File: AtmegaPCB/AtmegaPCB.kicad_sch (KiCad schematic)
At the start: 19 parts

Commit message: Matrix done!
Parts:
- added D? (x74): SOD-123, symbol Device:D_Small
- added D?: (no value), symbol Device:D_Small
- added MX? (x74): MX-NoLED, symbol MX_Alps_Hybrid:MX-NoLED
- added MX?: (no value), symbol MX_Alps_Hybrid:MX-NoLED
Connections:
- new net: D?.2 (A), MX?.2 (ROW) (x75)
- new net COL0: MX?.1 (COL), MX?.1 (COL), MX?.1 (COL), MX?.1 (COL), MX?.1 (COL)
- new net COL1: MX?.1 (COL), MX?.1 (COL), MX?.1 (COL), MX?.1 (COL), MX?.1 (COL)
- new net COL10: MX?.1 (COL), MX?.1 (COL), MX?.1 (COL), MX?.1 (COL), MX?.1 (COL)
- new net COL11: MX?.1 (COL), MX?.1 (COL), MX?.1 (COL), MX?.1 (COL)
- new net COL12: MX?.1 (COL), MX?.1 (COL), MX?.1 (COL), MX?.1 (COL)
- new net COL13: MX?.1 (COL), MX?.1 (COL), MX?.1 (COL), MX?.1 (COL)
- new net COL14: MX?.1 (COL), MX?.1 (COL), MX?.1 (COL)
- new net COL15: MX?.1 (COL), MX?.1 (COL)
- new net COL16: MX?.1 (COL), MX?.1 (COL)
- new net COL17: MX?.1 (COL)
- new net COL2: MX?.1 (COL), MX?.1 (COL), MX?.1 (COL), MX?.1 (COL), MX?.1 (COL)
- new net COL3: MX?.1 (COL), MX?.1 (COL), MX?.1 (COL), MX?.1 (COL), MX?.1 (COL)
- new net COL4: MX?.1 (COL), MX?.1 (COL), MX?.1 (COL), MX?.1 (COL), MX?.1 (COL)
- new net COL5: MX?.1 (COL), MX?.1 (COL), MX?.1 (COL), MX?.1 (COL), MX?.1 (COL)
- new net COL6: MX?.1 (COL), MX?.1 (COL), MX?.1 (COL), MX?.1 (COL), MX?.1 (COL)
- new net COL7: MX?.1 (COL), MX?.1 (COL), MX?.1 (COL), MX?.1 (COL), MX?.1 (COL)
- new net COL8: MX?.1 (COL), MX?.1 (COL), MX?.1 (COL), MX?.1 (COL), MX?.1 (COL)
- new net COL9: MX?.1 (COL), MX?.1 (COL), MX?.1 (COL), MX?.1 (COL), MX?.1 (COL)
- new net ROW0: D?.1 (K), D?.1 (K), D?.1 (K), D?.1 (K), D?.1 (K), D?.1 (K), D?.1 (K), D?.1 (K), D?.1 (K), D?.1 (K), D?.1 (K), D?.1 (K), D?.1 (K), D?.1 (K), D?.1 (K), D?.1 (K), D?.1 (K), D?.1 (K)
- new net ROW1: D?.1 (K), D?.1 (K), D?.1 (K), D?.1 (K), D?.1 (K), D?.1 (K), D?.1 (K), D?.1 (K), D?.1 (K), D?.1 (K), D?.1 (K), D?.1 (K), D?.1 (K), D?.1 (K), D?.1 (K), D?.1 (K), D?.1 (K)
- new net ROW2: D?.1 (K), D?.1 (K), D?.1 (K), D?.1 (K), D?.1 (K), D?.1 (K), D?.1 (K), D?.1 (K), D?.1 (K), D?.1 (K), D?.1 (K), D?.1 (K), D?.1 (K), D?.1 (K)
- new net ROW3: D?.1 (K), D?.1 (K), D?.1 (K), D?.1 (K), D?.1 (K), D?.1 (K), D?.1 (K), D?.1 (K), D?.1 (K), D?.1 (K), D?.1 (K), D?.1 (K), D?.1 (K), D?.1 (K), D?.1 (K)
- new net ROW4: D?.1 (K), D?.1 (K), D?.1 (K), D?.1 (K), D?.1 (K), D?.1 (K), D?.1 (K), D?.1 (K), D?.1 (K), D?.1 (K), D?.1 (K)
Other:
- moved on the sheet: C?, F?, R?, SW?, U?, USB?, Y?

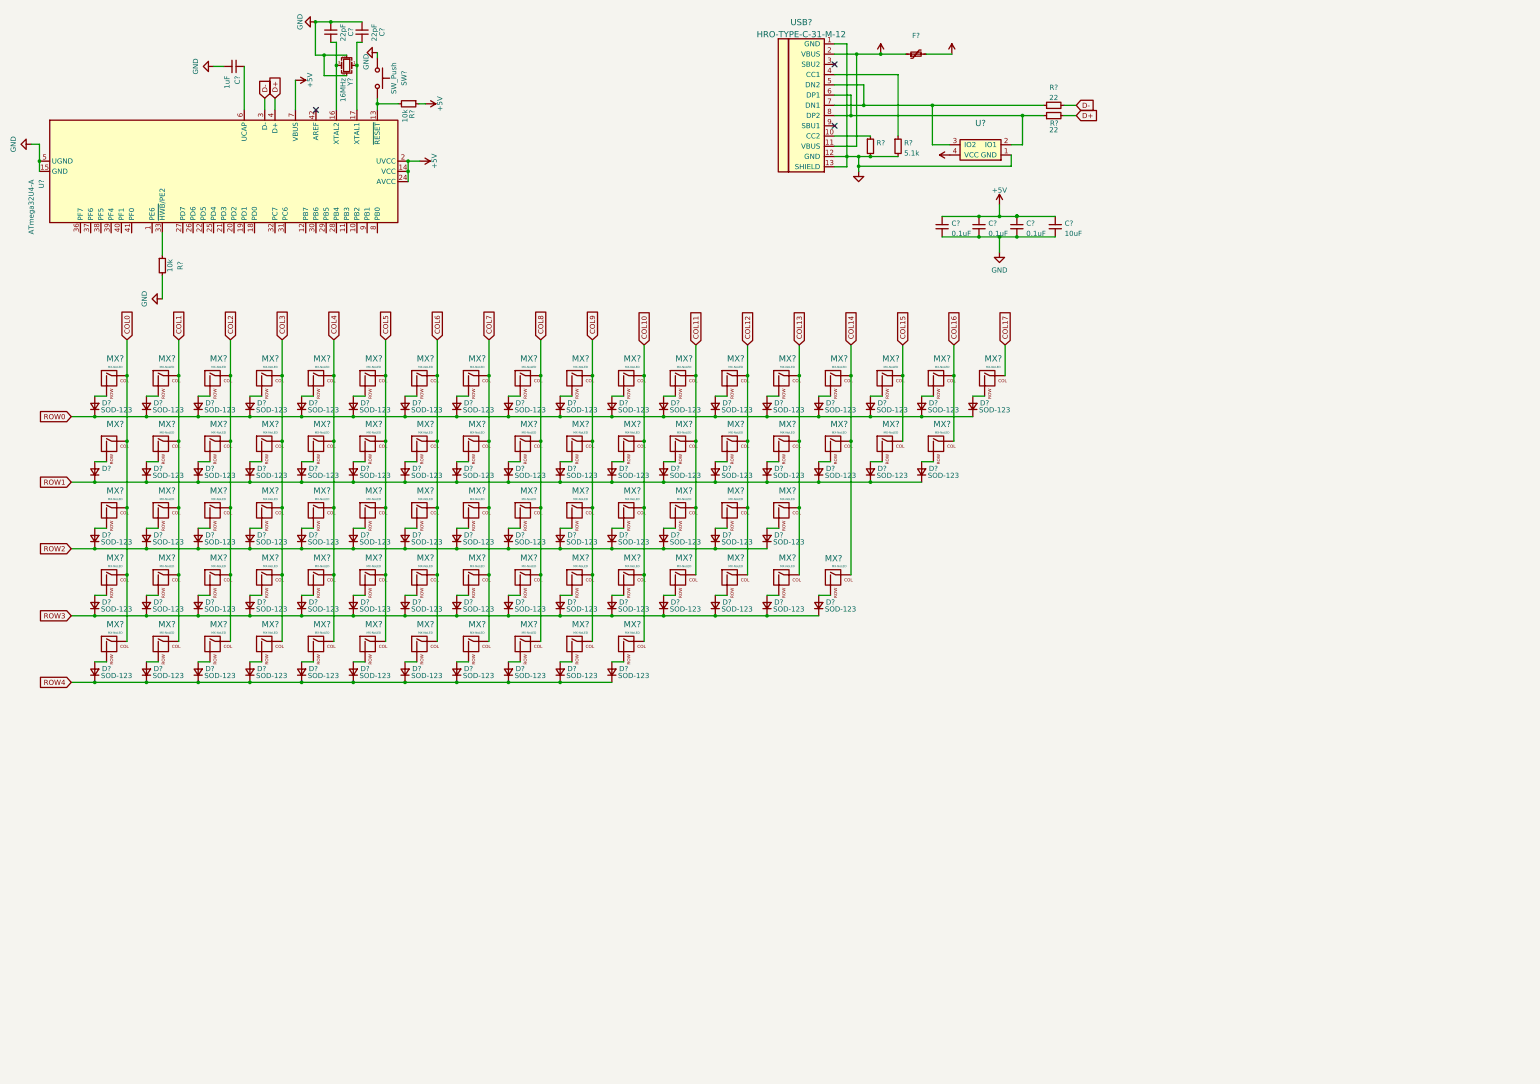
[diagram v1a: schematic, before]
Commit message: Added footprints
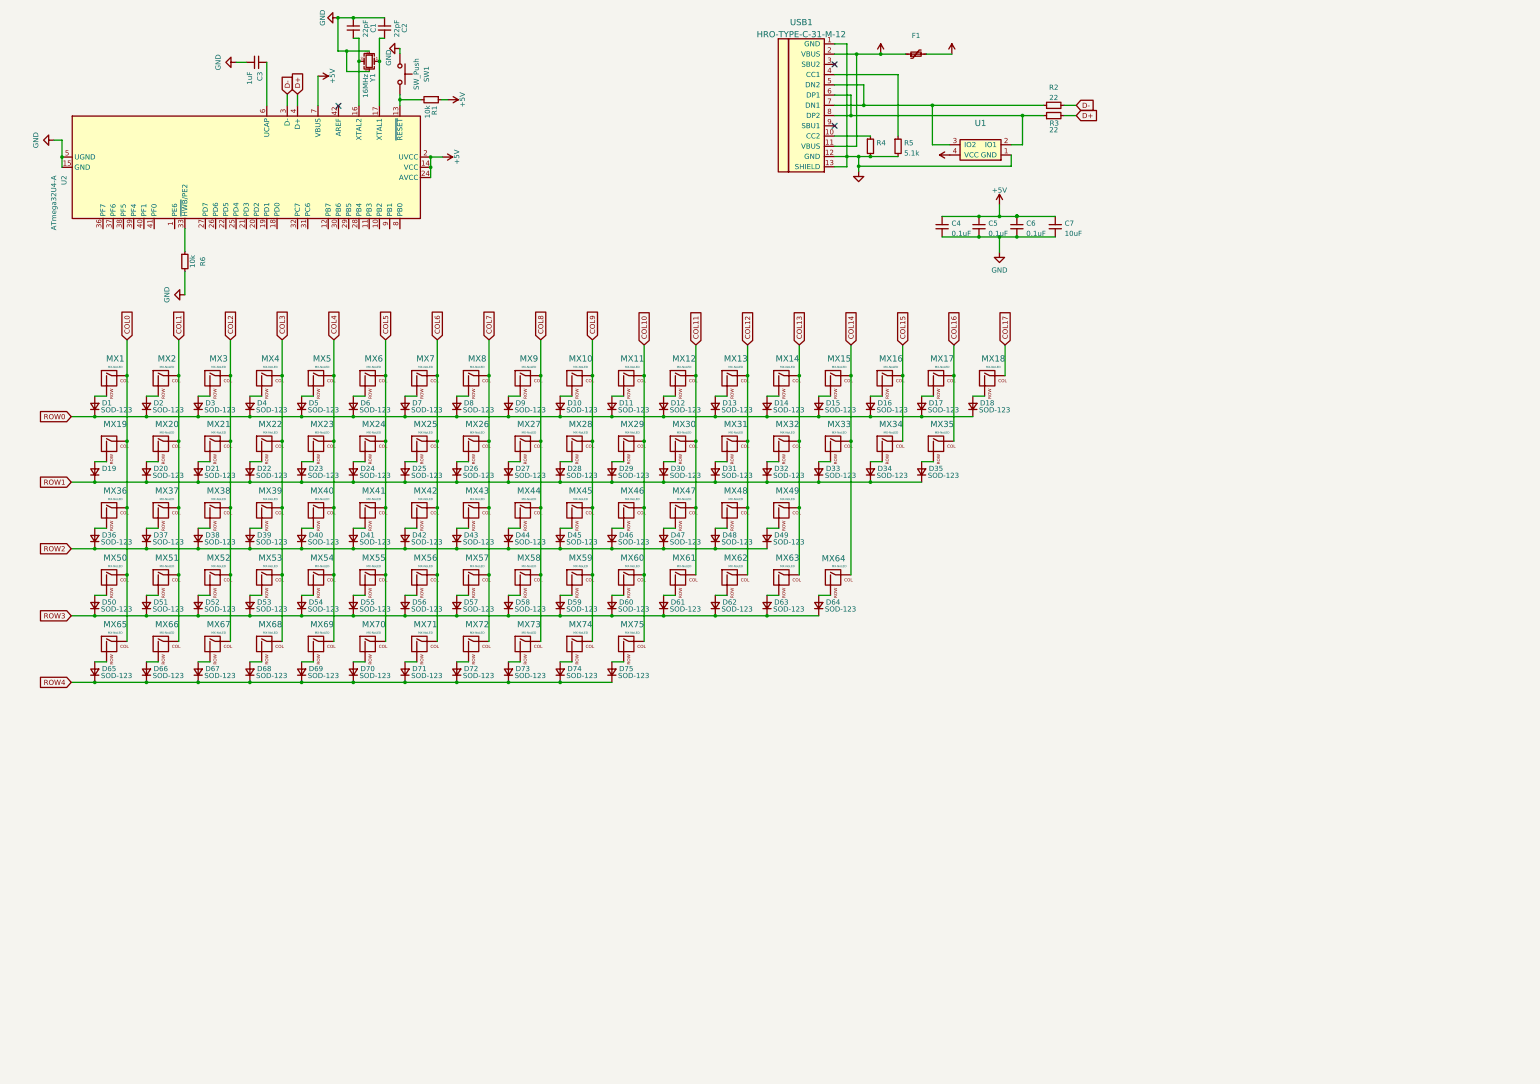
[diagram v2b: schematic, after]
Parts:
- gave numbers to parts that had none: 169
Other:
- moved on the sheet: C1, C2, C3, R1, R6, SW1, U2, Y1

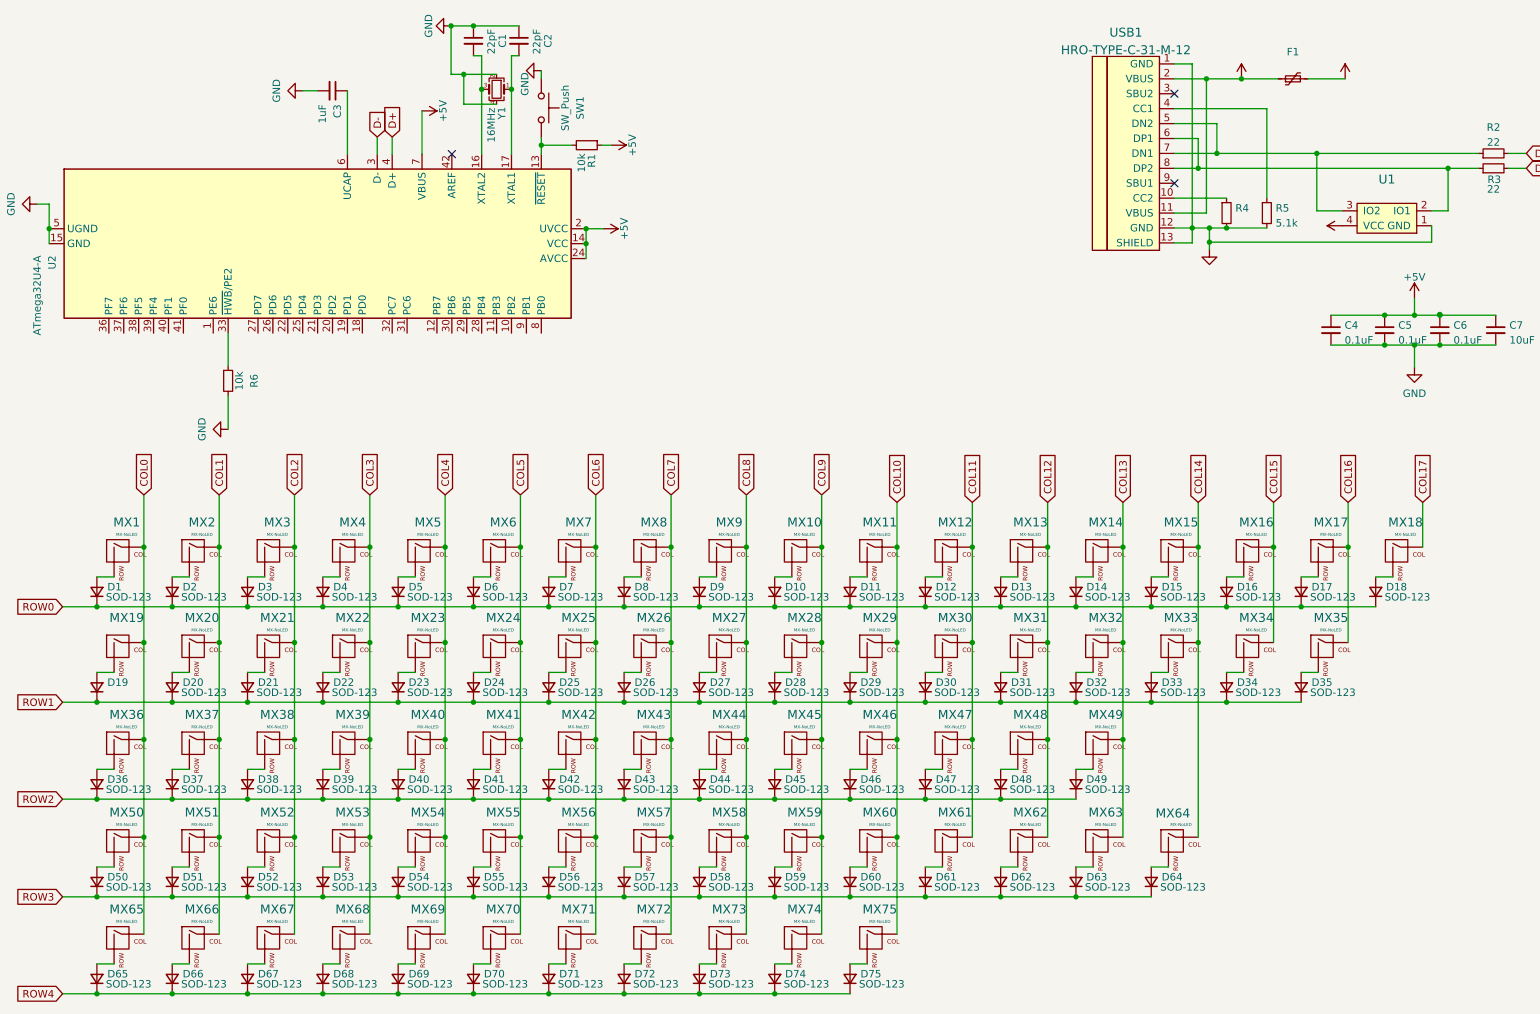
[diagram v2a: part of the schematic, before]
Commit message: Added missed keys
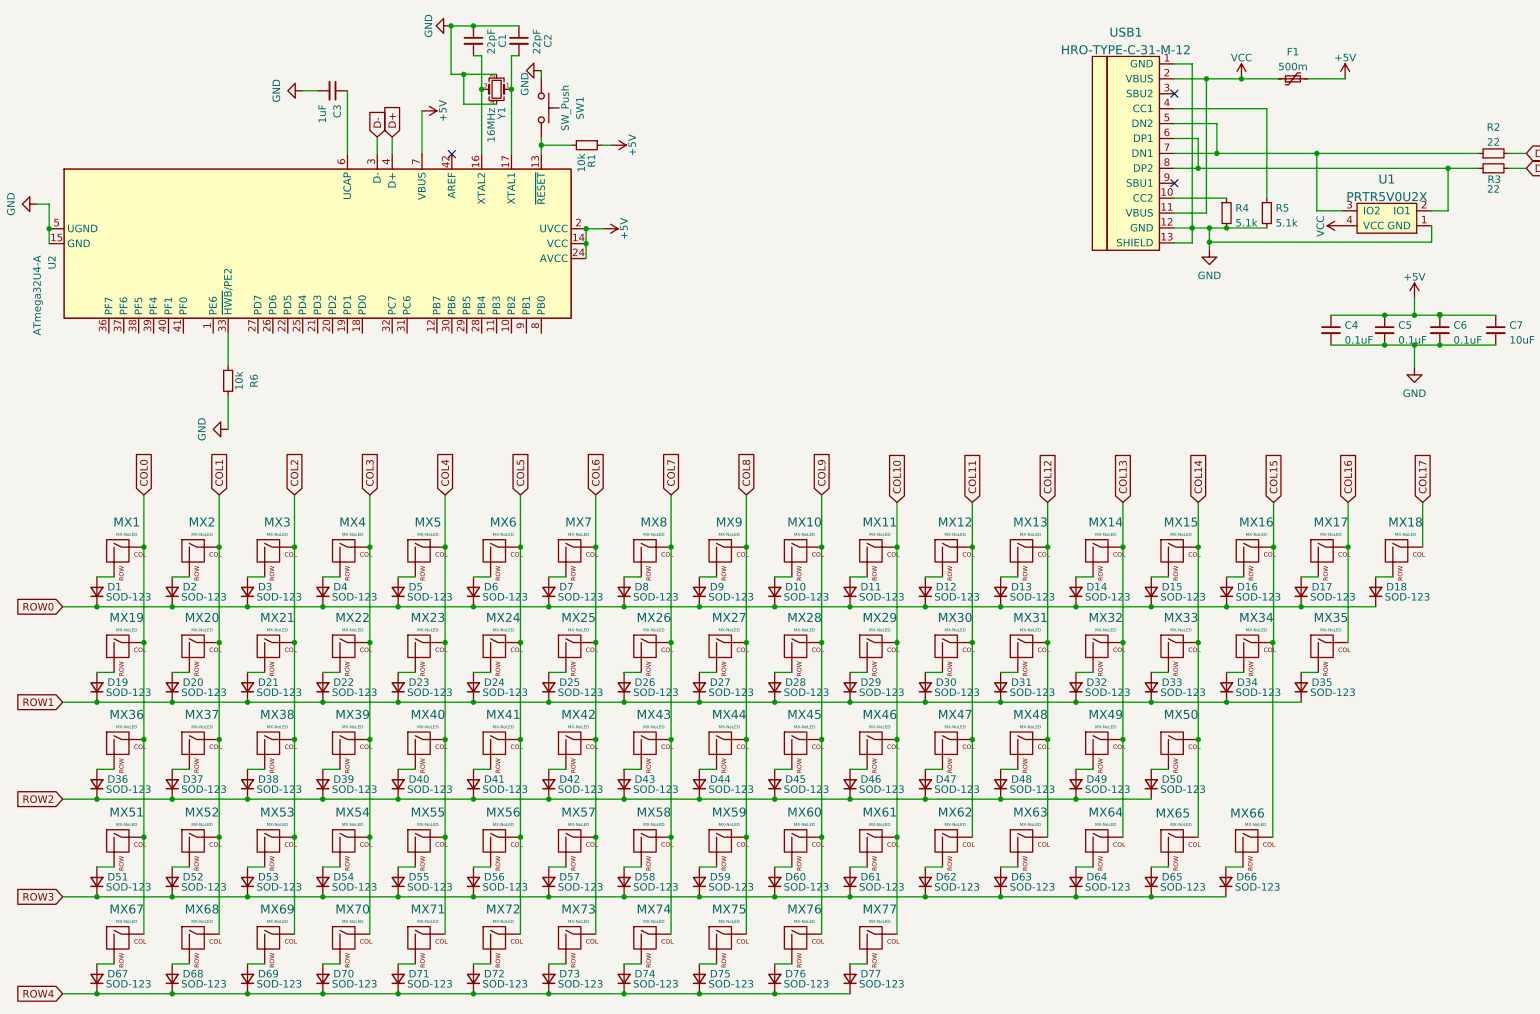
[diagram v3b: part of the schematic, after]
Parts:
- added D50, D66: SOD-123, Diode_SMD:D_SOD-123, symbol Device:D_Small
- added MX50: (no value), symbol MX_Alps_Hybrid:MX-NoLED
- added MX66: MX-NoLED, MX_Alps_Hybrid:MX-1U-NoLED, symbol MX_Alps_Hybrid:MX-NoLED
- C1, C2, C3, C4, C5, C6, C7: footprint (none) -> Capacitor_SMD:C_0805_2012Metric
- D1, D10, D11, D12, D13, D14, D15, D16, D17, D18, D2, D20, D21, D22, D23, D24, D25, D26, D27, D28, D29, D3, D30, D31, D32, D33, D34, D35, D36, D37, D38, D39, D4, D40, D41, D42, D43, D44, D45, D46, D47, D48, D49, D5, D6, D7, D8, D9: footprint (none) -> Diode_SMD:D_SOD-123
- D19: value (none) -> SOD-123; footprint (none) -> Diode_SMD:D_SOD-123
- D51: renamed from D50; footprint (none) -> Diode_SMD:D_SOD-123
- D52: renamed from D51; footprint (none) -> Diode_SMD:D_SOD-123
- D53: renamed from D52; footprint (none) -> Diode_SMD:D_SOD-123
- D54: renamed from D53; footprint (none) -> Diode_SMD:D_SOD-123
- D55: renamed from D54; footprint (none) -> Diode_SMD:D_SOD-123
- D56: renamed from D55; footprint (none) -> Diode_SMD:D_SOD-123
- D57: renamed from D56; footprint (none) -> Diode_SMD:D_SOD-123
- D58: renamed from D57; footprint (none) -> Diode_SMD:D_SOD-123
- D59: renamed from D58; footprint (none) -> Diode_SMD:D_SOD-123
- D60: renamed from D59; footprint (none) -> Diode_SMD:D_SOD-123
- D61: renamed from D60; footprint (none) -> Diode_SMD:D_SOD-123
- D62: renamed from D61; footprint (none) -> Diode_SMD:D_SOD-123
- D63: renamed from D62; footprint (none) -> Diode_SMD:D_SOD-123
- D64: renamed from D63; footprint (none) -> Diode_SMD:D_SOD-123
- D65: renamed from D64; footprint (none) -> Diode_SMD:D_SOD-123
- D67: renamed from D65; footprint (none) -> Diode_SMD:D_SOD-123
- D68: renamed from D66; footprint (none) -> Diode_SMD:D_SOD-123
- D69: renamed from D67; footprint (none) -> Diode_SMD:D_SOD-123
- D70: renamed from D68; footprint (none) -> Diode_SMD:D_SOD-123
- D71: renamed from D69; footprint (none) -> Diode_SMD:D_SOD-123
- D72: renamed from D70; footprint (none) -> Diode_SMD:D_SOD-123
- D73: renamed from D71; footprint (none) -> Diode_SMD:D_SOD-123
- D74: renamed from D72; footprint (none) -> Diode_SMD:D_SOD-123
- D75: renamed from D73; footprint (none) -> Diode_SMD:D_SOD-123
- D76: renamed from D74; footprint (none) -> Diode_SMD:D_SOD-123
- D77: renamed from D75; footprint (none) -> Diode_SMD:D_SOD-123
- F1: value (none) -> 500m; footprint (none) -> Fuse:Fuse_1206_3216Metric
- MX1, MX10, MX11, MX12, MX13, MX14, MX15, MX17, MX18, MX2, MX20, MX21, MX22, MX23, MX24, MX25, MX26, MX27, MX28, MX29, MX3, MX30, MX31, MX32, MX33, MX34, MX35, MX36, MX37, MX39, MX4, MX40, MX41, MX42, MX43, MX44, MX45, MX46, MX47, MX48, MX49, MX5, MX6, MX7, MX8, MX9: footprint (none) -> MX_Alps_Hybrid:MX-1U-NoLED
- MX19: value (none) -> MX-NoLED; footprint (none) -> MX_Alps_Hybrid:MX-1U-NoLED
- MX51: renamed from MX50; footprint (none) -> MX_Alps_Hybrid:MX-1U-NoLED
- MX52: renamed from MX51; footprint (none) -> MX_Alps_Hybrid:MX-1U-NoLED
- MX54: renamed from MX53; footprint (none) -> MX_Alps_Hybrid:MX-1U-NoLED
- MX55: renamed from MX54; footprint (none) -> MX_Alps_Hybrid:MX-1U-NoLED
- MX56: renamed from MX55; footprint (none) -> MX_Alps_Hybrid:MX-1U-NoLED
- MX57: renamed from MX56; footprint (none) -> MX_Alps_Hybrid:MX-1U-NoLED
- MX58: renamed from MX57; footprint (none) -> MX_Alps_Hybrid:MX-1U-NoLED
- MX59: renamed from MX58; footprint (none) -> MX_Alps_Hybrid:MX-1U-NoLED
- MX60: renamed from MX59; footprint (none) -> MX_Alps_Hybrid:MX-1U-NoLED
- MX61: renamed from MX60; footprint (none) -> MX_Alps_Hybrid:MX-1U-NoLED
- MX62: renamed from MX61; footprint (none) -> MX_Alps_Hybrid:MX-1U-NoLED
- MX63: renamed from MX62; footprint (none) -> MX_Alps_Hybrid:MX-1U-NoLED
- MX64: renamed from MX63; footprint (none) -> MX_Alps_Hybrid:MX-1U-NoLED
- MX67: renamed from MX65; footprint (none) -> MX_Alps_Hybrid:MX-1U-NoLED
- MX68: renamed from MX66; footprint (none) -> MX_Alps_Hybrid:MX-1U-NoLED
- MX76: renamed from MX74; footprint (none) -> MX_Alps_Hybrid:MX-1U-NoLED
- MX77: renamed from MX75; footprint (none) -> MX_Alps_Hybrid:MX-1U-NoLED
- R1, R2, R3, R5, R6: footprint (none) -> Resistor_SMD:R_0805_2012Metric
- R4: value (none) -> 5.1k; footprint (none) -> Resistor_SMD:R_0805_2012Metric
- SW1: footprint (none) -> random-keyboard-parts:SKQG-1155865
- U1: value (none) -> PRTR5V0U2X; footprint (none) -> Package_QFP:TQFP-44_10x10mm_P0.8mm
- USB1: footprint (none) -> Type-C:HRO-TYPE-C-31-M-12-Assembly
- Y1: footprint (none) -> Crystal:Crystal_SMD_3225-4Pin_3.2x2.5mm
- renumbered MX52 to MX53, MX64 to MX65, MX67 to MX69, MX68 to MX70, MX69 to MX71, MX70 to MX72, MX71 to MX73, MX72 to MX74, MX73 to MX75
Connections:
- net COL14: now also MX50.1 (COL)
- net ROW2: now also D50.1 (K)
- net ROW3: now also D66.1 (K)
- new net: D66.2 (A), MX66.2 (ROW)
- new net: D50.2 (A), MX50.2 (ROW)

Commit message: Update
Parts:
- removed D50, D66: SOD-123, Diode_SMD:D_SOD-123, symbol Device:D_Small
- removed MX50: (no value), symbol MX_Alps_Hybrid:MX-NoLED
- removed MX66: MX-NoLED, MX_Alps_Hybrid:MX-1U-NoLED, symbol MX_Alps_Hybrid:MX-NoLED
- added D36, D39, D78: SOD-123, Diode_SMD:D_SOD-123, symbol Device:D_Small
- added MX36, MX78: MX-NoLED, MX_Alps_Hybrid:MX-1U-NoLED, symbol MX_Alps_Hybrid:MX-NoLED
- added MX39: (no value), symbol MX_Alps_Hybrid:MX-NoLED
- MX16: footprint (none) -> MX_Alps_Hybrid:MX-2U-NoLED
- MX21, MX34: footprint MX_Alps_Hybrid:MX-1U-NoLED -> (none)
- MX35: value MX-NoLED -> (none); footprint MX_Alps_Hybrid:MX-1U-NoLED -> (none)
- MX51: renamed from MX49; footprint MX_Alps_Hybrid:MX-1U-NoLED -> (none)
- MX54: renamed from MX53; footprint (none) -> MX_Alps_Hybrid:MX-2.25U-NoLED
- MX66: renamed from MX65; footprint (none) -> MX_Alps_Hybrid:MX-2.75U-NoLED
- MX69, MX70, MX71, MX73, MX74, MX75: footprint (none) -> MX_Alps_Hybrid:MX-1.25U-NoLED
- MX72: footprint (none) -> MX_Alps_Hybrid:MX-6.25U-ReversedStabilizers-NoLED
- renumbered D36 to D37, D37 to D38, D38 to D40, D39 to D41, D40 to D42, D41 to D43, D42 to D44, D43 to D45, D44 to D46, D45 to D47, D46 to D48, D47 to D49, D48 to D50, D49 to D51, D51 to D52, D52 to D53, D53 to D54, D54 to D55, D55 to D56, D56 to D57, D57 to D58, D58 to D59, D59 to D60, D60 to D61, D61 to D62, D62 to D63, D63 to D64, D64 to D65, D65 to D66, MX36 to MX37, MX37 to MX38, MX38 to MX40, MX39 to MX41, MX40 to MX42, MX41 to MX43, MX42 to MX44, MX43 to MX45, MX44 to MX46, MX45 to MX47, MX46 to MX48, MX47 to MX49, MX48 to MX50, MX51 to MX52, MX52 to MX53, MX54 to MX55, MX55 to MX56, MX56 to MX57, MX57 to MX58, MX58 to MX59, MX59 to MX60, MX60 to MX61, MX61 to MX62, MX62 to MX63, MX63 to MX64, MX64 to MX65
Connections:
- net COL10: now also MX47.1 (COL); no longer MX48.1 (COL)
- net COL11: now also MX48.1 (COL), MX78.1 (COL); no longer MX49.1 (COL)
- net COL12: now also MX49.1 (COL); no longer MX50.1 (COL)
- net COL13: now also MX50.1 (COL); no longer MX51.1 (COL)
- net COL14: now also MX51.1 (COL)
- net COL16: no longer MX17.1 (COL), MX35.1 (COL)
- net COL17: now also MX36.1 (COL)
- net COL2: now also MX39.1 (COL); no longer MX40.1 (COL)
- net COL3: now also MX40.1 (COL); no longer MX41.1 (COL)
- net COL4: now also MX41.1 (COL); no longer MX42.1 (COL)
- net COL5: now also MX42.1 (COL); no longer MX43.1 (COL)
- net COL6: now also MX43.1 (COL); no longer MX44.1 (COL)
- net COL7: now also MX44.1 (COL); no longer MX45.1 (COL)
- net COL8: now also MX45.1 (COL); no longer MX46.1 (COL)
- net COL9: now also MX46.1 (COL); no longer MX47.1 (COL)
- net ROW1: now also D36.1 (K)
- net ROW2: now also D39.1 (K)
- net ROW4: now also D78.1 (K)
- new net: D78.2 (A), MX78.2 (ROW)
- new net: D36.2 (A), MX36.2 (ROW)
- new net: D39.2 (A), MX39.2 (ROW)
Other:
- moved on the sheet: D40, D41, D42, D43, D44, D45, D46, D47, D48, D49, D50, D51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
